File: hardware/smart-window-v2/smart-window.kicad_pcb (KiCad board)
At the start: 2 copper layers, 57 parts, among them J1 Screw_Terminal_01x02, J10 Conn_01x06_Pin, J11 Conn_02x03_Odd_Even, J12 Conn_01x04_Socket, J13 Conn_01x04_Socket, J14 Conn_01x05_Pin, J15 Conn_01x03_Socket, J2 12V INPUT, J3 Screw_Terminal_01x02, J4 Conn_01x03_Socket, J5 Conn_01x03_Socket, J6 Screw_Terminal_01x02, J7 Conn_01x04_Socket, J8 Conn_01x04_Socket, J9 Conn_01x04_Socket, SW1 SW_Push_Dual, SW2 SW_Push_Dual, U1 TSDP341xx, U2 DHT11, U3 L7805, U4 ATmega328P-P, Y1 16MHz

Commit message: Schematic Completed
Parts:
- removed D3: 1N47xxA, Diode_THT:D_DO-41_SOD81_P10.16mm_Horizontal
- removed J1: Screw_Terminal_01x02, TerminalBlock:TerminalBlock_bornier-2_P5.08mm
- removed PS1: HLK-5M05, Converter_ACDC:Converter_ACDC_Hi-Link_HLK-5Mxx
- added FID1: Fiducial, Fiducial:Fiducial_1mm_Mask2mm, F.Cu at (243.7, 85.8)
- added FID2: Fiducial, Fiducial:Fiducial_1mm_Mask2mm, F.Cu at (243.7, 89.4)
- added FID3: Fiducial, Fiducial:Fiducial_1mm_Mask2mm, F.Cu at (243.7, 92.9)
- added H1: MountingHole, MountingHole:MountingHole_4.3mm_M4, F.Cu at (171.2, 64.2)
- added H2: MountingHole, MountingHole:MountingHole_4.3mm_M4, F.Cu at (80.6, 64.9)
- added H3: MountingHole, MountingHole:MountingHole_4.3mm_M4, F.Cu at (171.4, 152.9)
- added H4: MountingHole, MountingHole:MountingHole_4.3mm_M4, F.Cu at (81.0, 153.7)

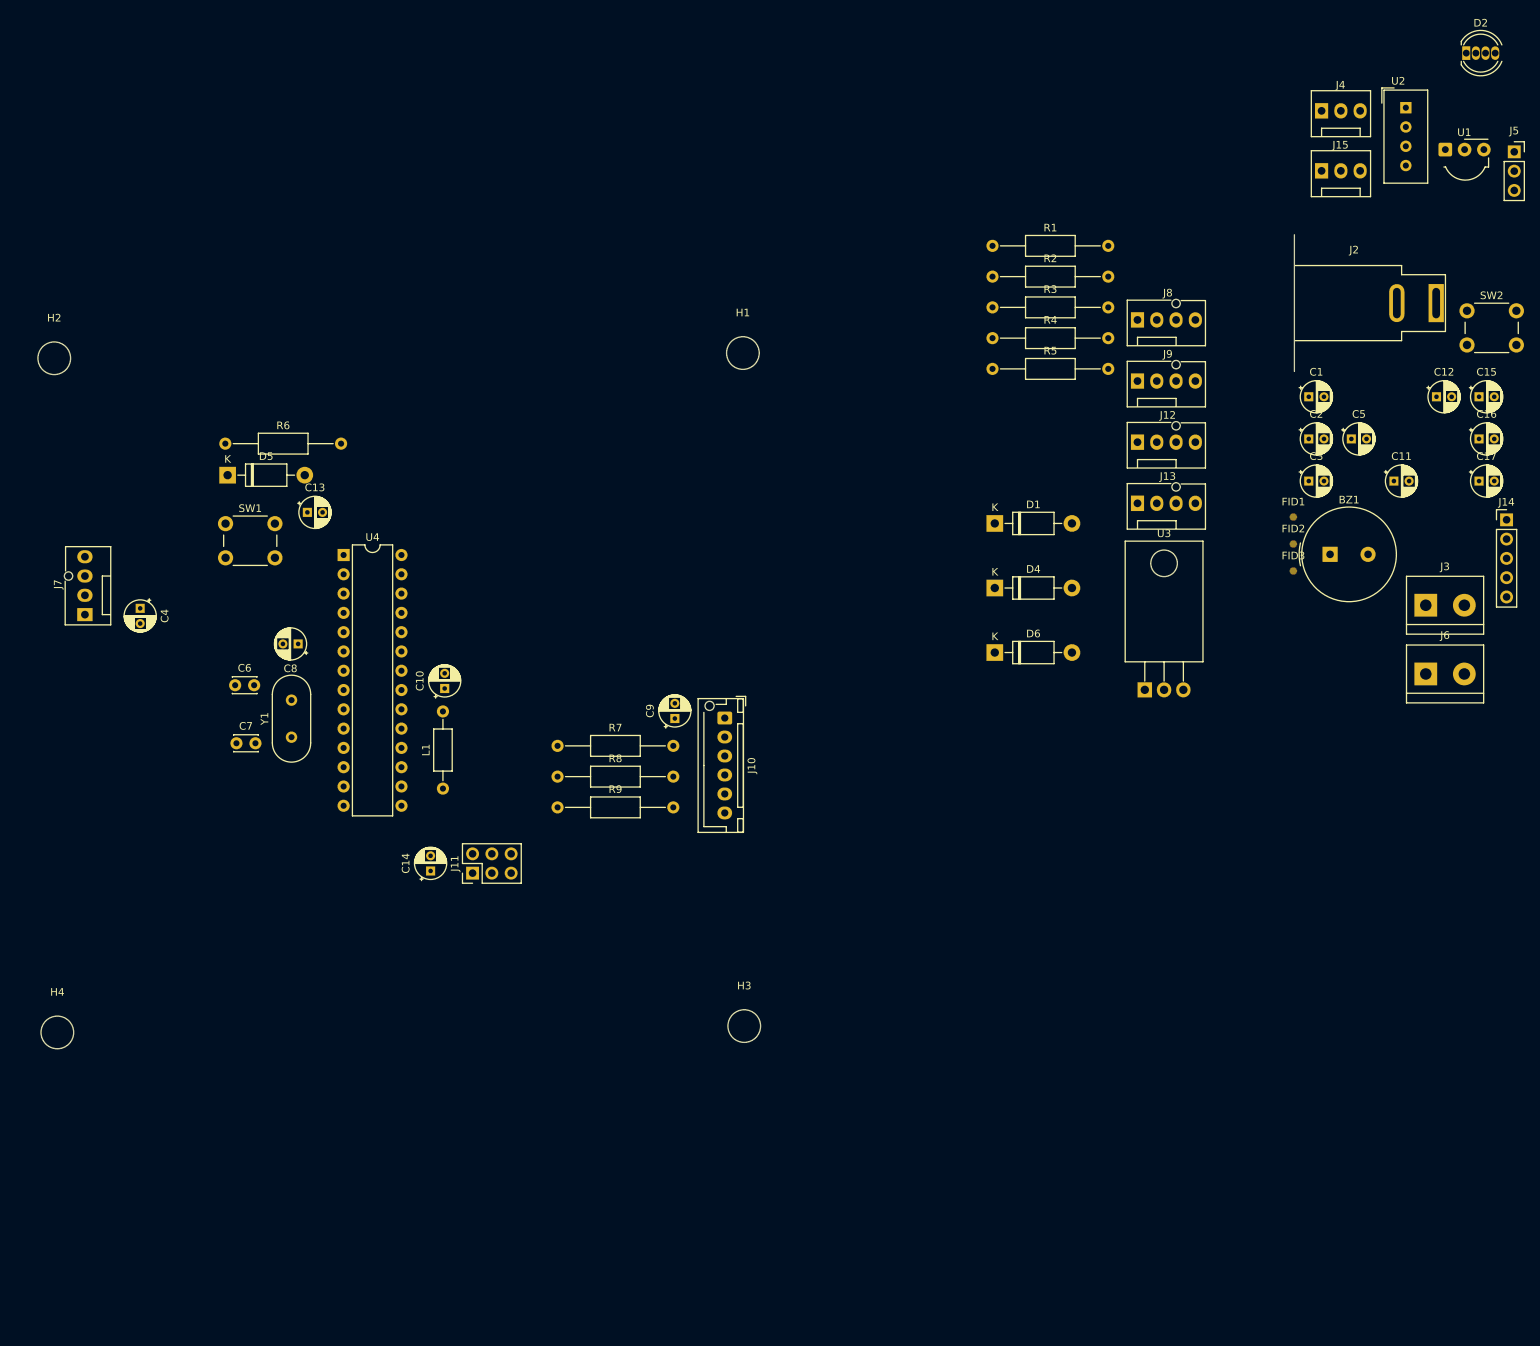
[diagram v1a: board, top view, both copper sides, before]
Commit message: Draft of PCB Arragement Complete
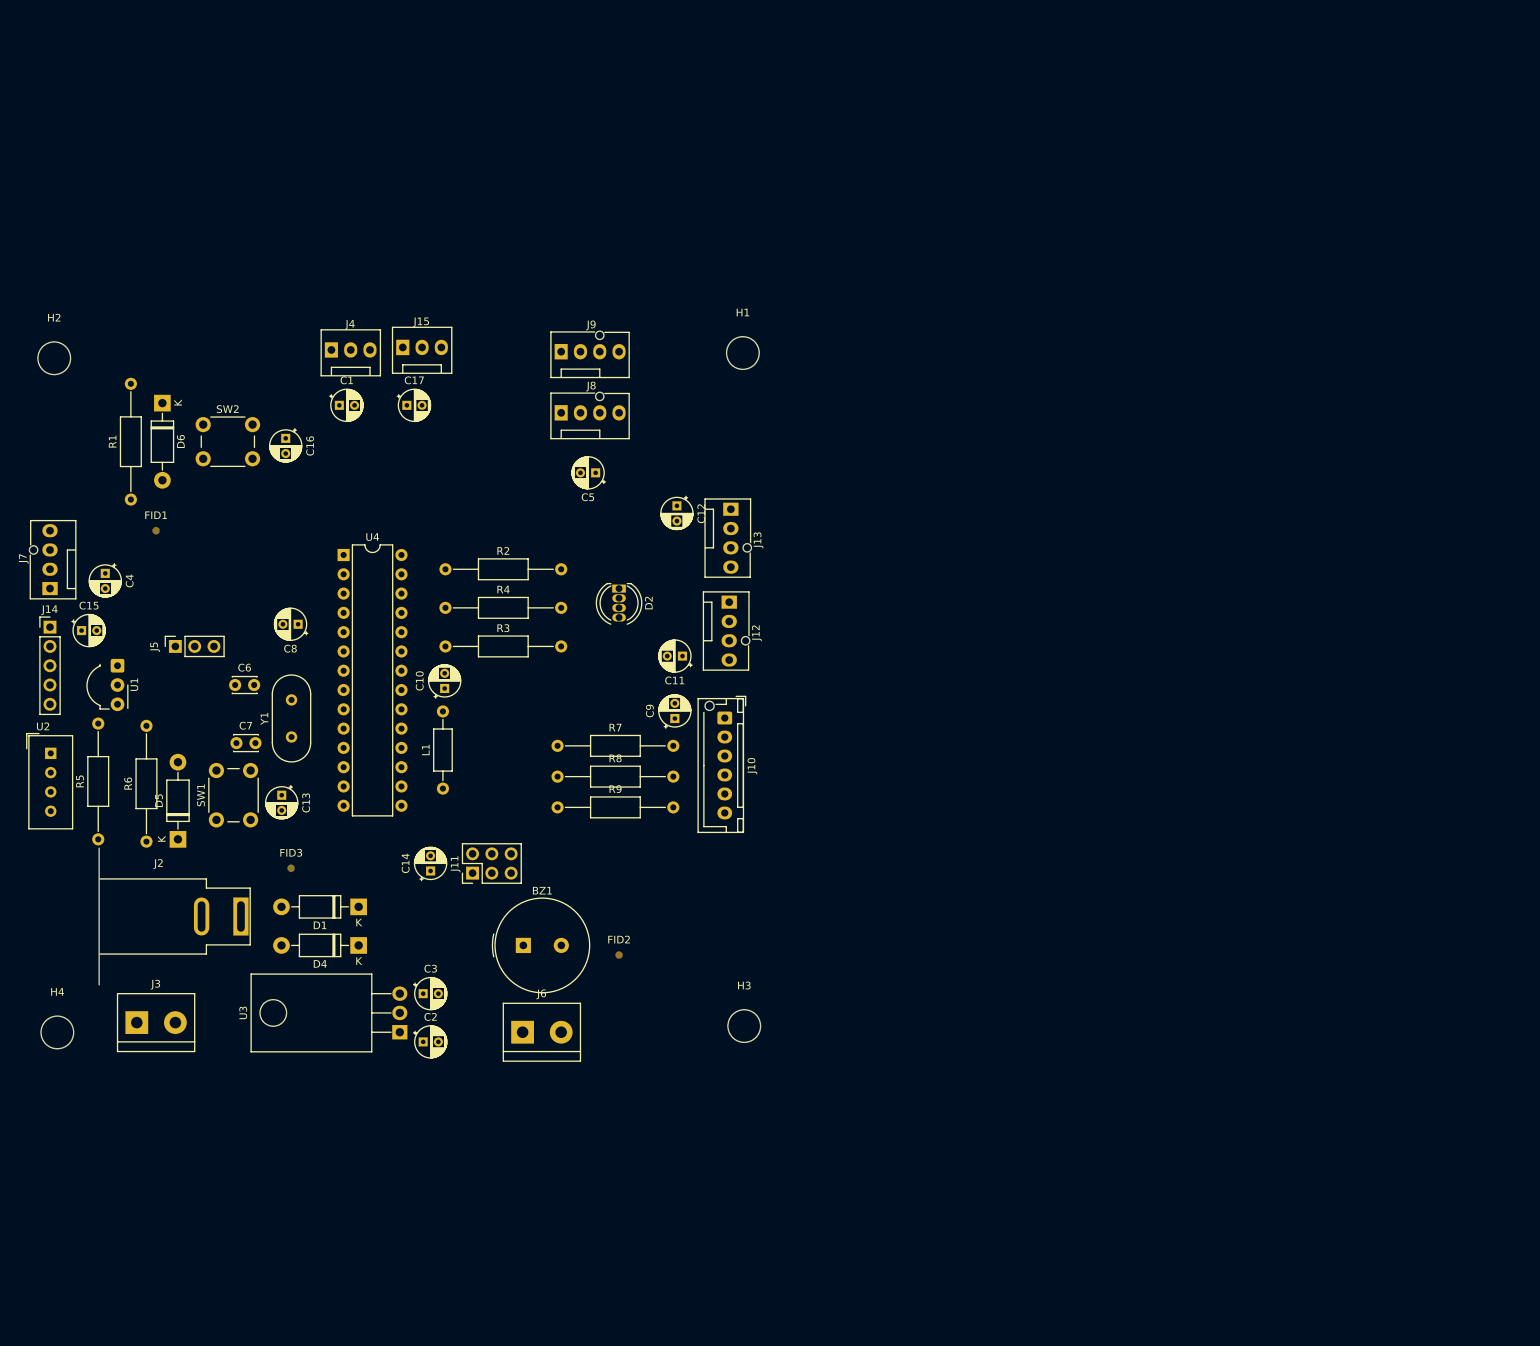
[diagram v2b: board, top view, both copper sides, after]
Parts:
- moved U2 197.7 mm to (80.1, 116.9)
- moved J14 192.3 mm to (80.0, 100.3)
- moved J5 187.9 mm to (96.5, 102.9), turned to 90 degrees
- moved U1 187.6 mm to (88.9, 105.4), turned to -90 degrees
- moved C15 186.6 mm to (84.2, 100.8)
- moved J3 178.4 mm to (91.4, 152.4)
- moved J2 176.9 mm to (105.2, 138.4)
- moved SW2 167.1 mm to (100.2, 73.7)
- moved C16 157.1 mm to (111.0, 75.5), turned to -90 degrees
- moved FID1 149.8 mm to (94.0, 87.6)
- moved C17 141.5 mm to (127.0, 71.1)
- moved C2 141.1 mm to (129.2, 154.9)
- moved FID3 137.7 mm to (111.8, 132.1)
- moved C3 134.7 mm to (129.2, 148.6)
- moved J4 134.1 mm to (117.1, 63.8)
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
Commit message: pcb design silkscreen in progress
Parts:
- removed C12, C17: 100nF 25V, Capacitor_THT:CP_Radial_D4.0mm_P2.00mm
- removed D1, D6: 1N47xxA, Diode_THT:D_DO-41_SOD81_P10.16mm_Horizontal
- removed H4: MountingHole, MountingHole:MountingHole_4.3mm_M4
- removed J13: Conn_01x04_Socket, Connector:FanPinHeader_1x04_P2.54mm_Vertical
- removed J15: Conn_01x03_Socket, Connector:FanPinHeader_1x03_P2.54mm_Vertical
- removed R7, R8, R9: 330R 1/4W, Resistor_THT:R_Axial_DIN0207_L6.3mm_D2.5mm_P15.24mm_Horizontal
- added D3: 1N47xxA, Diode_THT:D_DO-41_SOD81_P10.16mm_Horizontal, B.Cu at (125.5, 145.8)
- added J1: Barrel_Jack_MountingPin, Connector_BarrelJack:BarrelJack_Horizontal, F.Cu at (114.1, 142.1)
- added JP1: SolderJumperOpen, Jumper:SolderJumper-2_P1.3mm_Open_TrianglePad1.0x1.5mm, F.Cu at (148.1, 68.8)
- added JP2: SolderJumperOpen, Jumper:SolderJumper-2_P1.3mm_Open_TrianglePad1.0x1.5mm, F.Cu at (144.5, 103.1)
- added JP3: SolderJumperOpen, Jumper:SolderJumper-2_P1.3mm_Open_TrianglePad1.0x1.5mm, F.Cu at (119.6, 75.2)
- added REF**: OSHW-Symbol_6.7x6mm_SilkScreen, Symbol:OSHW-Symbol_6.7x6mm_SilkScreen, F.Cu at (134.1, 66.3)
- added TP1: TestPoint, PCM_4ms_TestPoint:TestPoint_Pad_04, F.Cu at (122.2, 145.8)
- added TP2: TestPoint, PCM_4ms_TestPoint:TestPoint_Pad_04, F.Cu at (141.2, 87.6)
- added TP3: TestPoint, PCM_4ms_TestPoint:TestPoint_Pad_04, F.Cu at (156.0, 127.5)
- added TP4: TestPoint, PCM_4ms_TestPoint:TestPoint_Pad_04, F.Cu at (136.1, 124.0)
- added TP5: TestPoint, PCM_4ms_TestPoint:TestPoint_Pad_04, F.Cu at (149.2, 75.2)
- added TP6: TestPoint, PCM_4ms_TestPoint:TestPoint_Pad_04, F.Cu at (149.1, 72.7)
- C2: value 330nF 25V -> 100nF 25V
- C3: value 100nF 25V -> 330nF 25V
- C6: value 12pF -> 100nF 25V; footprint Capacitor_THT:C_Disc_D3.0mm_W2.0mm_P2.50mm -> Capacitor_THT:CP_Radial_D4.0mm_P2.00mm
- C8: value 100nF 25V -> 12pF; footprint Capacitor_THT:CP_Radial_D4.0mm_P2.00mm -> Capacitor_THT:C_Disc_D3.0mm_W2.0mm_P2.50mm
- D4, D5, R2, R3, R5, R6, U3: moved to B.Cu
- J10: value Conn_01x06_Pin -> Conn_01x04_Socket; footprint Connector_JST:JST_XH_B6B-XH-AM_1x06_P2.50mm_Vertical -> Connector:FanPinHeader_1x04_P2.54mm_Vertical
- J11: value Conn_02x03_Odd_Even -> Conn_01x04_Socket; footprint Connector_PinHeader_2.54mm:PinHeader_2x03_P2.54mm_Vertical -> Connector:FanPinHeader_1x04_P2.54mm_Vertical
- J12: value Conn_01x04_Socket -> Screw_Terminal_01x02; footprint Connector:FanPinHeader_1x04_P2.54mm_Vertical -> TerminalBlock_Altech:Altech_AK100_1x02_P5.00mm
- J14: value Conn_01x05_Pin -> Screw_Terminal_01x02; footprint Connector_PinHeader_2.54mm:PinHeader_1x05_P2.54mm_Vertical -> TerminalBlock_Altech:Altech_AK100_1x02_P5.00mm
- J2: value 12V INPUT -> Conn_01x03_Socket; footprint Connector_BarrelJack:BarrelJack_SwitchcraftConxall_RAPC10U_Horizontal -> PCM_4ms_Connector:Pins_1x03_2.54mm_TH
- J3: footprint TerminalBlock:TerminalBlock_bornier-2_P5.08mm -> TerminalBlock_Altech:Altech_AK100_1x02_P5.00mm
- J4: footprint Connector:FanPinHeader_1x03_P2.54mm_Vertical -> PCM_4ms_Connector:Pins_1x03_2.54mm_TH
- J6: value Screw_Terminal_01x02 -> Conn_01x04_Socket; footprint TerminalBlock:TerminalBlock_bornier-2_P5.08mm -> Connector:FanPinHeader_1x04_P2.54mm_Vertical
- J8: value Conn_01x04_Socket -> Conn_02x03_Odd_Even; footprint Connector:FanPinHeader_1x04_P2.54mm_Vertical -> Connector_PinHeader_2.54mm:PinHeader_2x03_P2.54mm_Vertical
- J9: value Conn_01x04_Socket -> Conn_01x02; footprint Connector:FanPinHeader_1x04_P2.54mm_Vertical -> Connector_PinSocket_2.54mm:PinSocket_1x02_P2.54mm_Vertical
- R1: value 10K 1/4W -> 330R 1/4W; moved to B.Cu
- R4: value 330R 1/4W -> 10K 1/4W; moved to B.Cu
- SW1, SW2: value SW_Push_Dual -> SW_Push; footprint Button_Switch_THT:SW_PUSH_6mm -> Button_Switch_THT:SW_PUSH_6mm_H4.3mm
- U1: value TSDP341xx -> DHT11; footprint OptoDevice:Vishay_MOLD-3Pin -> Sensor:Aosong_DHT11_5.5x12.0_P2.54mm
- U2: value DHT11 -> TSDP341xx; footprint Sensor:Aosong_DHT11_5.5x12.0_P2.54mm -> OptoDevice:Vishay_MOLD-3Pin
- moved J6 90.9 mm to (113.0, 67.6), turned to -90 degrees
- moved U2 83.5 mm to (140.5, 59.3), turned to 180 degrees
- moved C2 79.7 mm to (156.4, 80.0), turned to 180 degrees
- moved J7 76.6 mm to (153.9, 75.2)
- moved C5 74.4 mm to (126.5, 149.9)
- moved C4 72.0 mm to (153.2, 122.4)
- moved R5 65.5 mm to (151.9, 127.9), turned to 180 degrees
- moved J3 64.3 mm to (154.0, 137.5), turned to 90 degrees
- moved SW2 57.1 mm to (125.9, 124.6), turned to -90 degrees
- moved C16 53.5 mm to (145.8, 116.1), turned to 0 degrees
- moved J2 53.0 mm to (121.2, 87.9)
- moved R1 52.9 mm to (141.6, 69.3), turned to 180 degrees
- moved D5 52.7 mm to (149.1, 121.2), turned to 180 degrees
- moved U1 51.0 mm to (130.3, 75.7), turned to 90 degrees
- moved FID2 46.1 mm to (110.7, 130.6)
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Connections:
- C13 pad 1: /MCU_RESET -> +5V
- C15 pad 1: +5V -> /MCU_RESET
- C16 pad 1: /IO_USER -> +5V
- C2 pad 1: VCC -> +5V
- C3 pad 1: +5V -> VCC
- C4 pad 1: +5V -> /IO_USER
- C6 pad 1: GND -> +5V
- C6 pad 2: /MCU_XTAL1 -> GND
- C7 pad 2: /MCU_XTAL2 -> /MCU_XTAL1
- C8 pad 1: +5V -> GND
- C8 pad 2: GND -> /MCU_XTAL2
- D2 pad 2: Net-(D2-RA) -> /RED_L
- D2 pad 3: Net-(D2-BA) -> /BLUE_L
- D2 pad 4: Net-(D2-GA) -> /GREEN_L
- D4 pad 1: VCC -> +5V
- D4 pad 2: Net-(D4-A) -> /IO_USER
- J10 pad 2: /MCU_SS -> GND
- J10 pad 3: /MOSI_R -> unconnected-(J10-Pin_3-Pad3)
- J10 pad 4: /MISO_R -> /AD2_RAIN
- J11 pad 1: /MCU_MISO -> /AD3_MQ2
- J11 pad 2: +5V -> unconnected-(J11-Pin_2-Pad2)
- J11 pad 3: /MCU_SCK -> GND
- J11 pad 4: /MCU_MOSI -> +5V
- J12 pad 1: +5V -> GND
- J12 pad 2: GND -> /IO_SERV_L
- J14 pad 1: /MCU_RESET -> /IO_SERV_R
- J14 pad 2: +5V -> GND
- J2 pad 1: Net-(D1-A) -> /IO_SERV_R
- J2 pad 2: GND -> +5V
- J3 pad 1: Net-(D4-A) -> /+VCC_BARREL
- J4 pad 1: /IO_SERV_R -> /IO_SERV_L
- J6 pad 1: /IO_BUZZ -> GND
- J6 pad 2: GND -> /MCU_RXD
- J7 pad 1: +5V -> /AD4/SDA
- J7 pad 2: /MCU_TXD -> /AD5/SCL
- J7 pad 3: /MCU_RXD -> /+I2C_JUMP
- J8 pad 1: /AD4/SDA -> /MCU_MISO
- J8 pad 2: /AD5/SCL -> +5V
- J8 pad 3: +5V -> /MCU_SCK
- J8 pad 4: GND -> /MCU_MOSI
- J9 pad 1: /AD4/SDA -> /MCU_SS
- J9 pad 2: /AD5/SCL -> GND
- R1 pad 1: /IO_USER -> /IO_LED_R
- R1 pad 2: +5V -> /RED_L
- R2 pad 1: /IO_LED_R -> /IO_LED_B
- R2 pad 2: Net-(D2-RA) -> /GREEN_L
- R3 pad 1: /IO_LED_B -> /IO_LED_G
- R3 pad 2: Net-(D2-GA) -> /BLUE_L
- R4 pad 1: /IO_LED_G -> /IO_DHT
- R4 pad 2: Net-(D2-BA) -> +5V
- R5 pad 1: /IO_DHT -> /IO_USER
- SW1 pad 1: /MCU_RESET -> GND
- SW1 pad 2: /MCU_RESET -> /IO_USER
- SW2 pad 1: /IO_USER -> GND
- SW2 pad 2: /IO_USER -> /MCU_RESET
- U1 pad 1: /IO_IR_REC -> +5V
- U1 pad 2: GND -> /IO_DHT
- U1 pad 3: +5V -> unconnected-(U1-NC-Pad3)
- U2 pad 1: +5V -> /IO_IR_REC
- U2 pad 2: /IO_DHT -> GND
- U2 pad 3: unconnected-(U2-NC-Pad3) -> +5V
- U4 pad 23: /IO_LED_B -> /IO_LED_G
- U4 pad 24: /IO_LED_G -> /IO_LED_B
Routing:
- net +5V: track 0.00 -> 120.5 mm, vias 0 -> 5
- net /MCU_RESET: track 0.00 -> 99.3 mm, vias 0 -> 1
- net /IO_USER: track 0.00 -> 75.7 mm
- net GND: track 0.00 -> 73.0 mm, vias 0 -> 12
- net /IO_SERV_R: track 0.00 -> 60.1 mm
- net /IO_IR_REC: track 0.00 -> 51.9 mm
- net /IO_DHT: track 0.00 -> 51.7 mm
- net /IO_LED_R: track 0.00 -> 46.7 mm
- net /+VCC_BARREL: track 0.00 -> 46.0 mm
- net /IO_LED_B: track 0.00 -> 32.1 mm
- net /IO_LED_G: track 0.00 -> 29.7 mm
- net /AD3_MQ2: track 0.00 -> 27.9 mm
- net /IO_SERV_L: track 0.00 -> 26.2 mm
- net /IO_PIR: track 0.00 -> 25.7 mm
- net /AD5/SCL: track 0.00 -> 24.6 mm
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- added copper zone on F.Cu, net +5V
- added copper zone on B.Cu, net GND
- added copper zone on F.Cu, net GND
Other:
- board outline added: 50 x 100.1 mm
- board text added: "ADC3"
- board text added: "I2C"
- board text added: "PCB_3D_BR_SW"
- board text added: "PCB_3D_TL_SW"
- board text added: "PIR"
- board text added: "RESET"
- board text added: "UART"
- board text added: "USER"

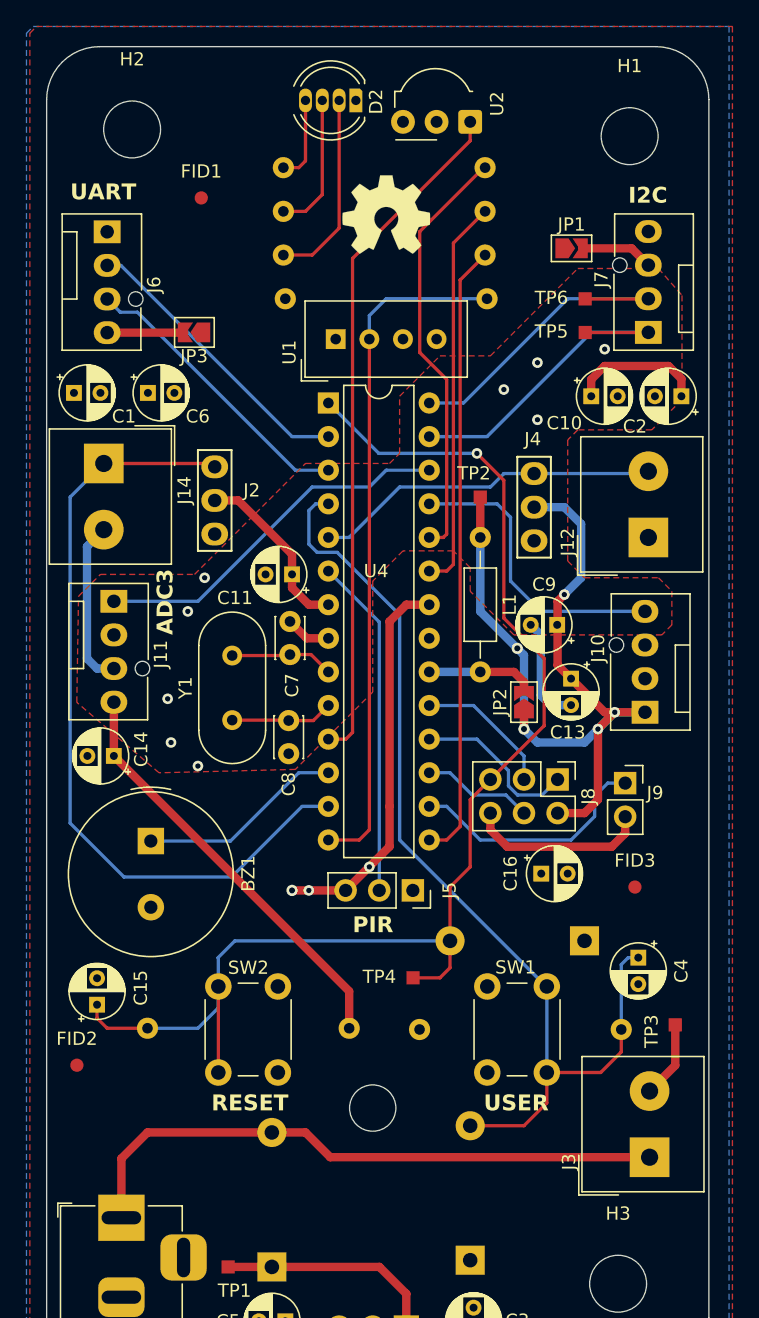
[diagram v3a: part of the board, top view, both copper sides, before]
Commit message: submitted files to jlc for manufacturing
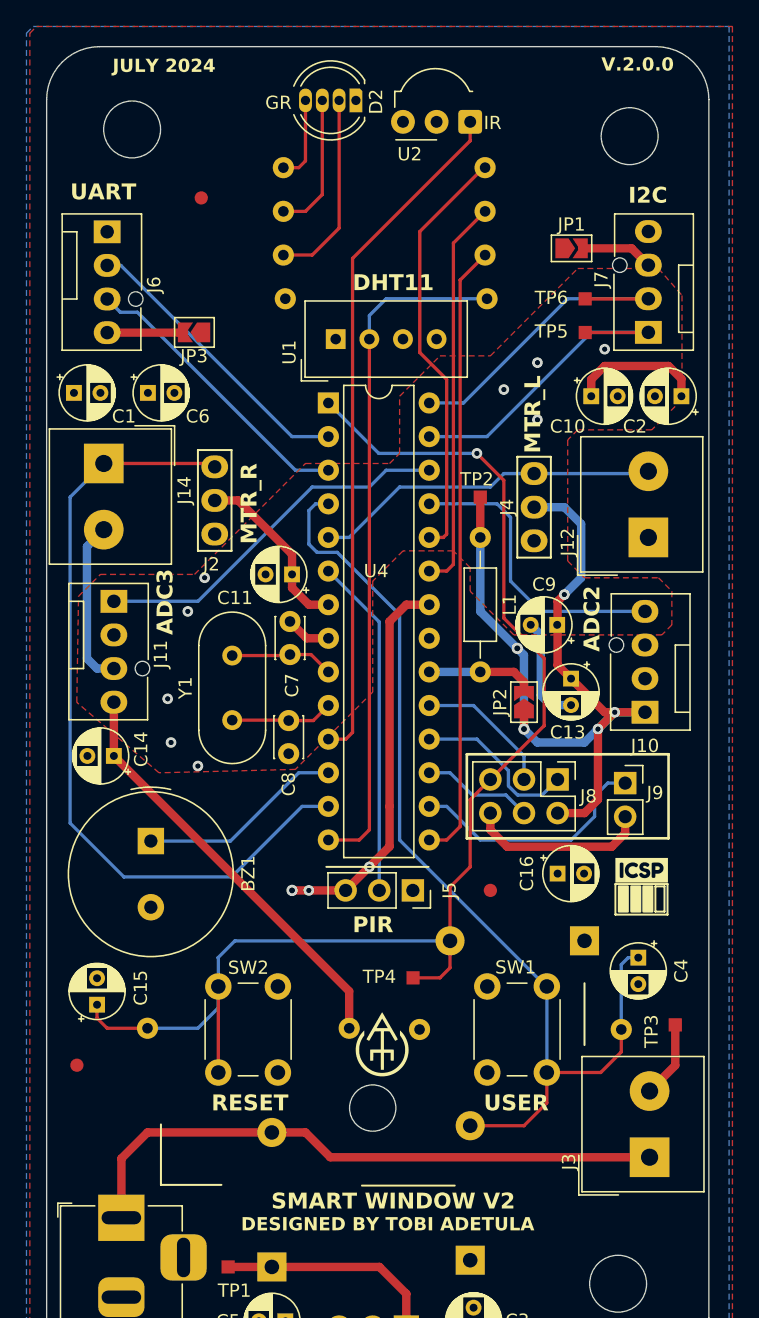
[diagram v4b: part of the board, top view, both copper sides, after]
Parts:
- removed the REF** at (134.1, 66.3)
- added G1: LOGO, Insignia:Insignia_mini, F.Cu at (133.8, 129.0)
- added G1: LOGO, Insignia:Insignia_mini, B.Cu at (133.9, 124.3)
- added REF**: Symbol_Barrel_Polarity, Symbol:Symbol_Barrel_Polarity, B.Cu at (110.7, 145.1)
- added REF**: WEEE-Logo_4.2x6mm_SilkScreen, Symbol:WEEE-Logo_4.2x6mm_SilkScreen, B.Cu at (146.2, 149.7)
- added REF**: KiCad-Logo2_5mm_SilkScreen, Symbol:KiCad-Logo2_5mm_SilkScreen, B.Cu at (146.8, 138.7)
- added kibuzzard-64D226C5: G***, kibuzzard-64D226C5, F.Cu at (153.4, 115.8)
- moved FID3 10.9 mm to (142.0, 117.3)
- moved C16 1.24 mm to (147.1, 116.1)
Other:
- board text added: "+"
- board text added: "+5V"
- board text added: "-"
- board text added: "10K"
- board text added: "220"
- board text added: "5V"
- board text added: "AD2"
- board text added: "AD3"
- board text added: "ADC2"
- board text added: "AVCC"
- board text added: "B"
- board text added: "BUZZ"
- board text added: "DESIGNED BY TOBI ADETULA"
- board text added: "DHT"
- board text added: "DHT11"
- board text added: "G"
- board text added: "GND"
- board text added: "GR"
- board text added: "IN"
- board text added: "IR"
- board text added: "JLCJLCJLCJLC"
- board text added: "JULY 2024"
- board text added: "MISO"
- board text added: "MOSI"
- board text added: "MQ"
- board text added: "MTR_L"
- board text added: "MTR_R"
- board text added: "ORDER NO"
- board text added: "OUT"
- board text added: "R"
- board text added: "RAIN"
- board text added: "RX"
- board text added: "SCK"
- board text added: "SCL"
- board text added: "SDA"
- board text added: "SDI"
- board text added: "SDO"
- board text added: "SERV_L"
- board text added: "SERV_R"
- board text added: "SMART WINDOW V2"
- board text added: "SS"
- board text added: "TX"
- board text added: "V.2.0.0"
